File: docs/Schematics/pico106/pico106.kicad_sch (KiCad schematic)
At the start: 18 parts, among them J1 MIDI in, J2 Debug, J3 Stereo line out, J4 Debug, J6 Stereo line out, SW1 RST, U1 Pico 2 (RP2350), U3 H11L1

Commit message: Update schematic
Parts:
- removed C1: 100nF, symbol Device:C
- removed C2, C4: 47uF, symbol Device:C_Polarized
- removed J6: Stereo line out, Connector_Audio:Jack_3.5mm_CUI_SJ1-3523N_Horizontal, symbol Connector_Audio:AudioJack2_Ground
- removed R19, R20: 220, Resistor_THT:R_Axial_DIN0204_L3.6mm_D1.6mm_P5.08mm_Horizontal, symbol Device:R
- removed R21: 1.8K, Resistor_THT:R_Axial_DIN0204_L3.6mm_D1.6mm_P5.08mm_Horizontal, symbol Device:R
- added C1: 47uF, symbol Device:C_Polarized
- added C2: 220pF, symbol Device:C
- added Q1: 2N2222A, Package_TO_SOT_THT:TO-39-3, symbol Transistor_BJT:2N2219
- added R3: 27k, Resistor_THT:R_Axial_DIN0204_L3.6mm_D1.6mm_P5.08mm_Horizontal, symbol Device:R
- added R4, R9: 33k, Resistor_THT:R_Axial_DIN0204_L3.6mm_D1.6mm_P5.08mm_Horizontal, symbol Device:R
- added R5: 220k, Resistor_THT:R_Axial_DIN0204_L3.6mm_D1.6mm_P5.08mm_Horizontal, symbol Device:R
- added R6: 1.8k, Resistor_THT:R_Axial_DIN0204_L3.6mm_D1.6mm_P5.08mm_Horizontal, symbol Device:R
- added R7: 47k, esistor_THT:R_Axial_DIN0204_L3.6mm_D1.6mm_P5.08mm_Horizontal, symbol Device:R
- added R8: 2.2k, Resistor_THT:R_Axial_DIN0204_L3.6mm_D1.6mm_P5.08mm_Horizontal, symbol Device:R
- added U2: TL072, symbol Amplifier_Operational:TL072
- C3: value 100nF -> 1nF
- R2: value 1.8K -> 33k
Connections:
- net Earth: now also J3.G, C1.2, R7.2, U2.3 (+), U2.5 (+); no longer C3.2, R2.1
- net MIDI 31250 baud 8-N-1: now also U1.26 (GPIO20); no longer U1.7 (GPIO5)
- net at U1.4 (GPIO2): now also C2.1
- net at U1.5 (GPIO3): now also R2.1
- net at C3.1: now also Q1.1 (E), R5.2, U2.2 (-)
- net at J3.T: now also R9.2
- net at R2.2: now also C1.1, R3.1
- new net: C2.2, R6.1, R7.1
- new net: C3.2, R8.2, R9.1, U2.1
- new net: R4.2, R5.1, U2.7
- new net: Q1.3 (C), R8.1
- new net: Q1.2 (B), R6.2
- new net: R3.2, R4.1, U2.6 (-)
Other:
- note added: "(1) Powered via micro USB connector on the Pico module (2) The Pico's USB connecTor acts as a USB MIDI-IN when running (3) Raspberry Pi Pico-1 (RP2040) also supported"
- note added: "DCO-1"
- note removed: "(1) Powered via micro USB connector on the Pico module (2) The Pico's USB interface acts as a USB MIDI-IN when running (3) Raspberry Pi Pico-1 (RP2040) also supported"
- note removed: "PWM DAC (ALTERNATIVE)"
- moved on the sheet: D1, J1, J2, J3, J4, R1, SW1, U1, U3

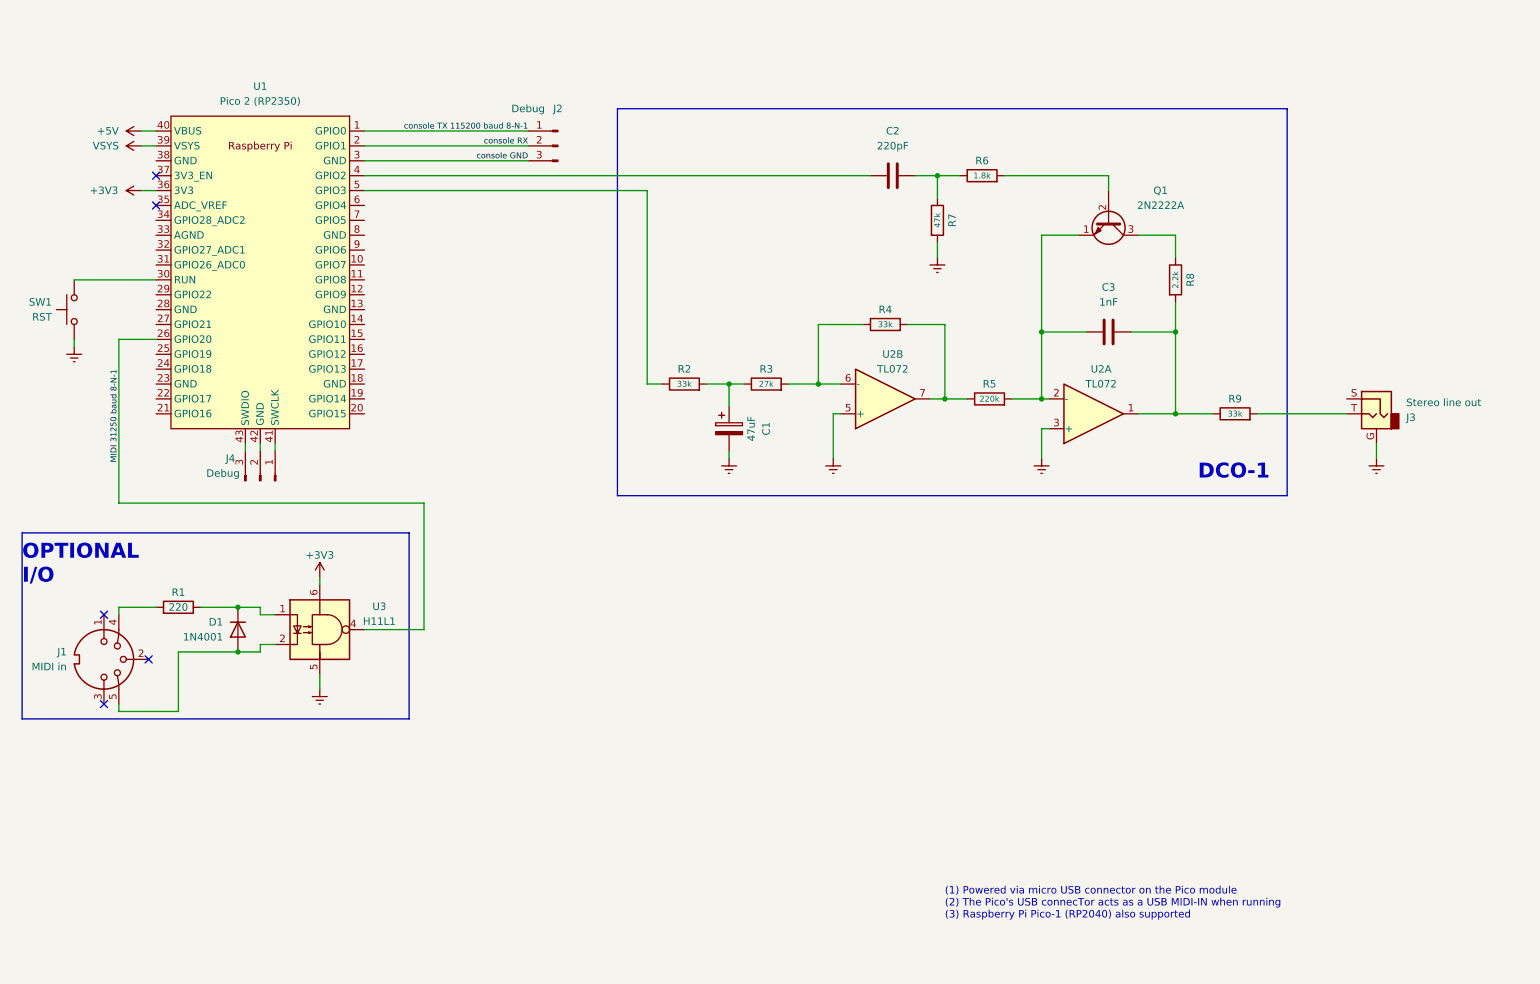
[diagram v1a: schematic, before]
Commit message: Move USB Midi device support into Platform for re-use
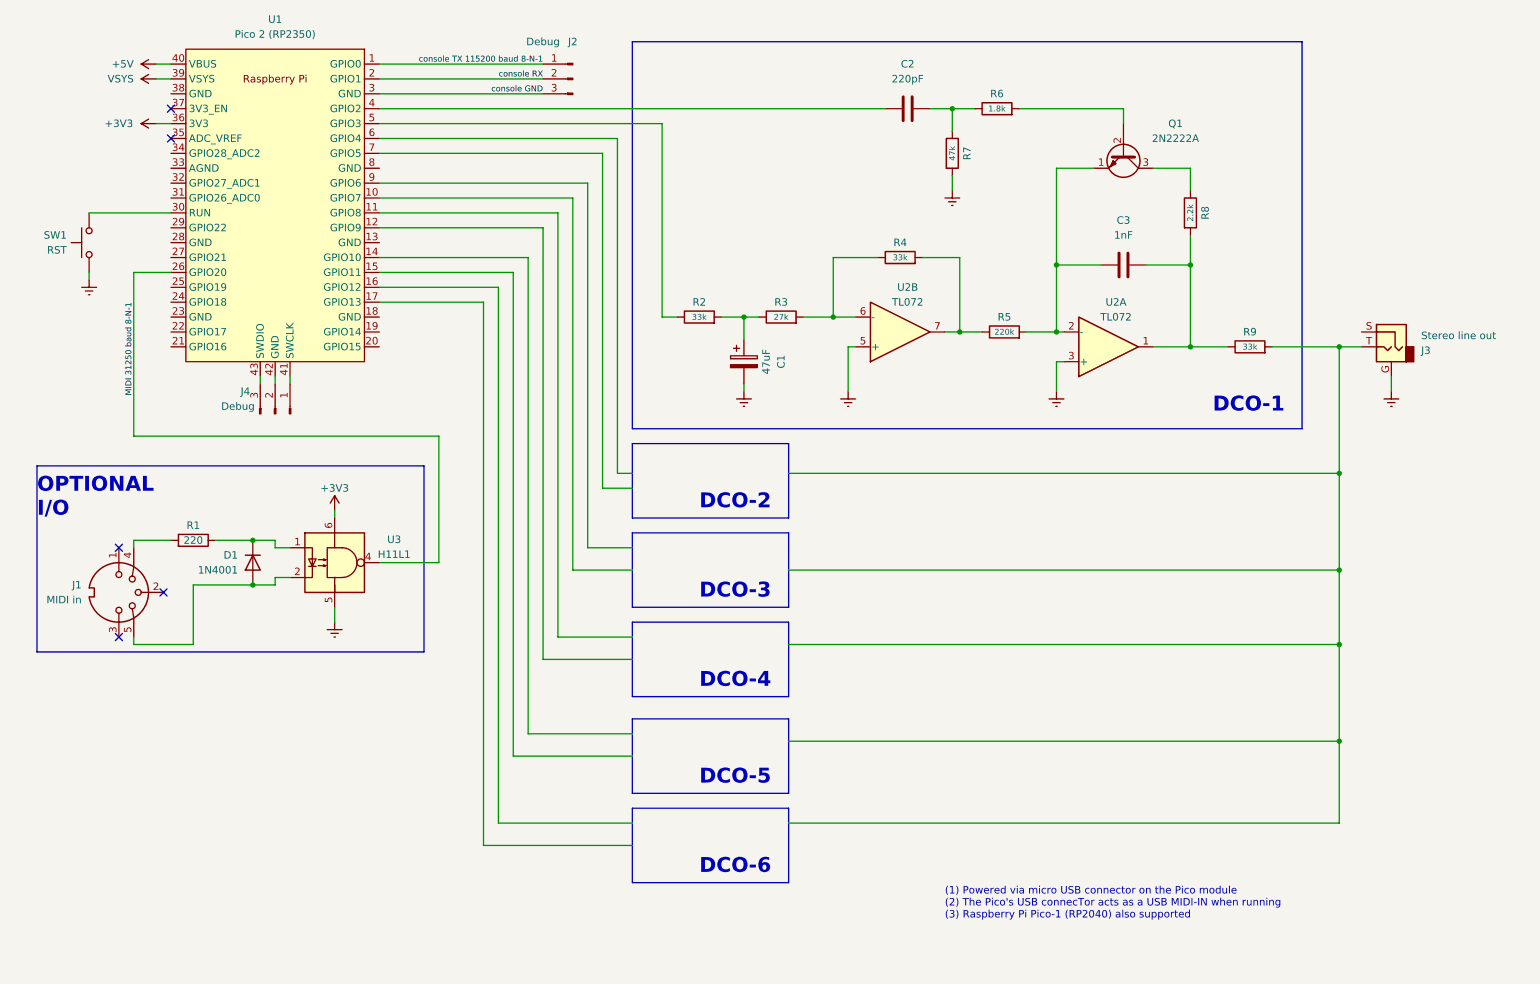
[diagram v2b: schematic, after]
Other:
- note added: "DCO-2"
- note added: "DCO-3"
- note added: "DCO-4"
- note added: "DCO-5"
- note added: "DCO-6"
- moved on the sheet: C1, C2, C3, D1, J1, J2, J3, J4, Q1, R1, R2, R3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
